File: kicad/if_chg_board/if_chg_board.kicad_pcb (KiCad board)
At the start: 2 copper layers, 62 x 26 mm, 46 parts, among them J1 USB_B_Micro, J2 B2B-ZH, J3 B2B-ZH, J4 Conn_01x05, Q1 SS8050-G, Q2 SS8050-G, SW1 B3U-1000P, SW2 B3U-1000P, U1 AMS1117-3.3, U2 LTC4054ES5-4.2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

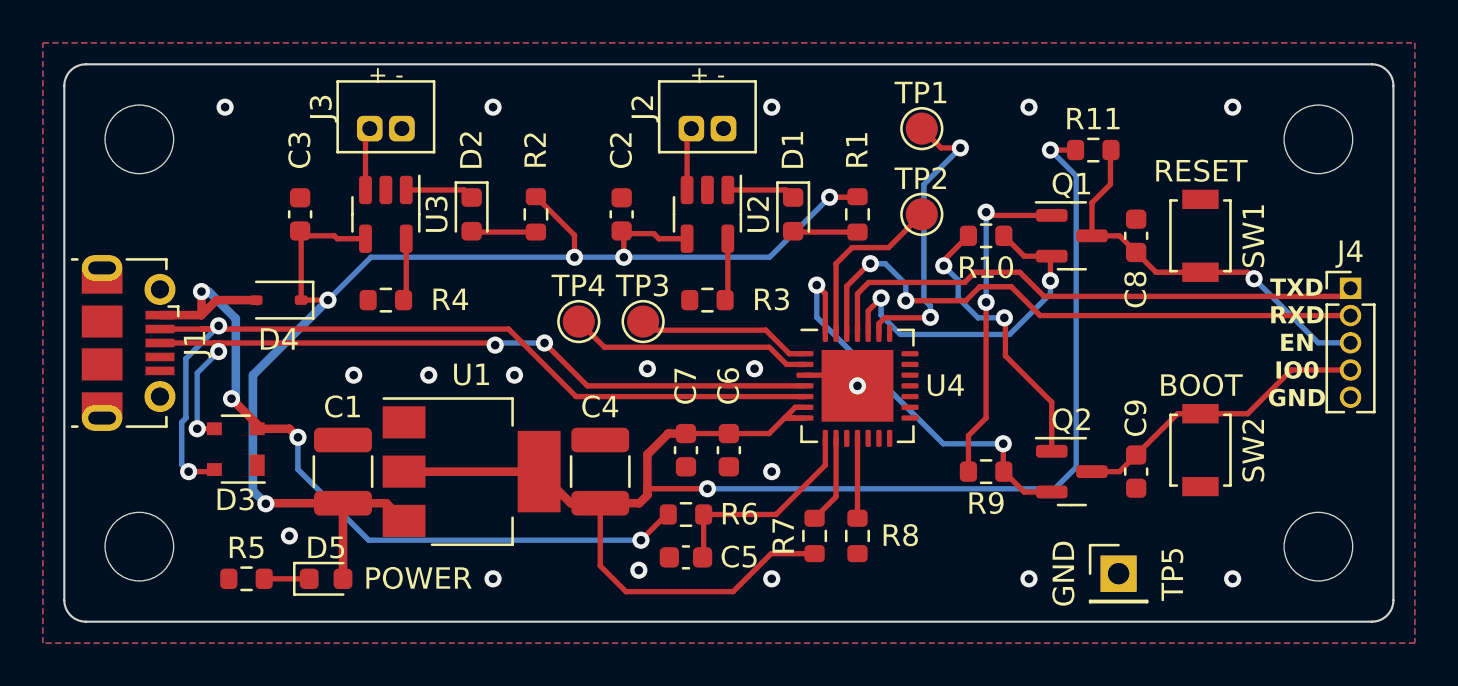
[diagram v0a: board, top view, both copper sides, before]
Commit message: Update if_chg_board
Signed-off-by: Kazuki Iida <elkel53930@gmail.com>
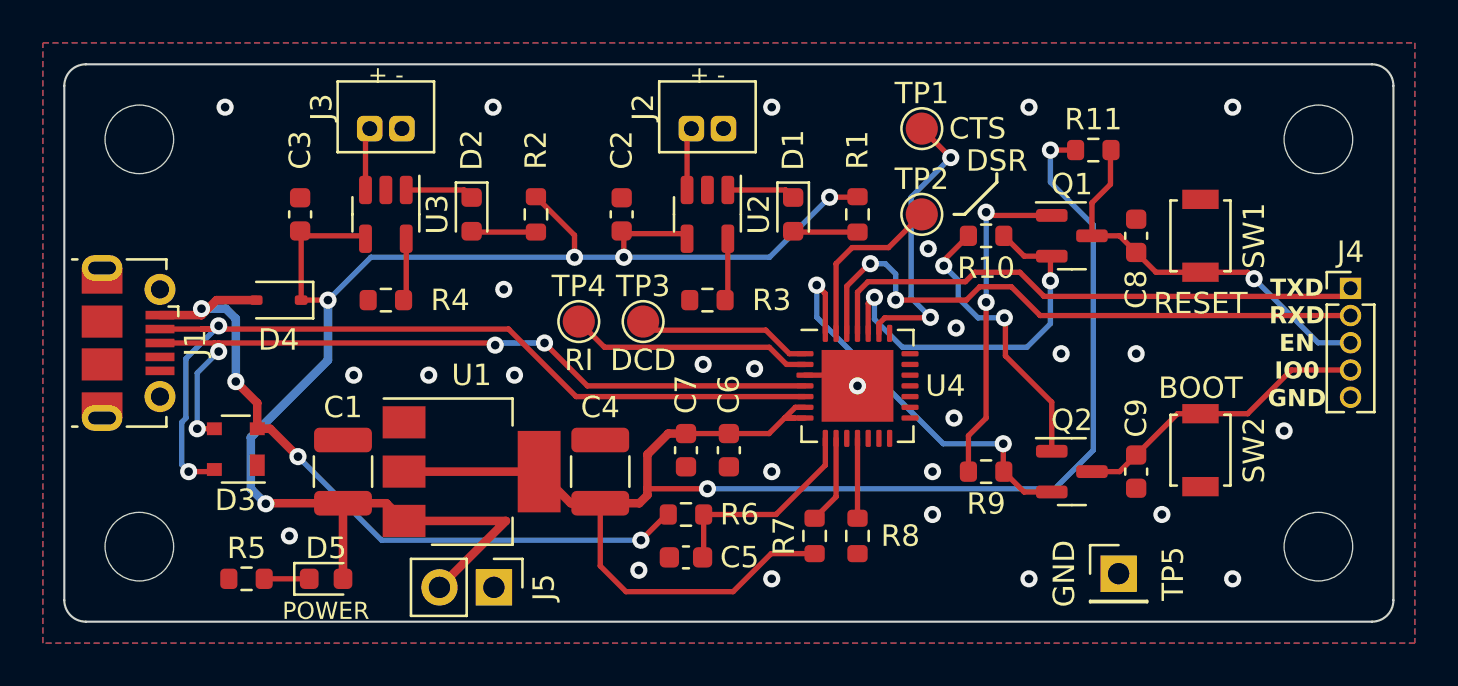
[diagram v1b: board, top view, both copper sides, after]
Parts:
- removed REF** (x4): MountingHole_3.2mm_M3, MountingHole:MountingHole_3.2mm_M3
- added H1: Φ3.2 M3, MountingHole:MountingHole_3.2mm_M3, F.Cu at (124.5, 91.5)
- added H2: Φ3.2 M3, MountingHole:MountingHole_3.2mm_M3, F.Cu at (124.5, 110.5)
- added H3: Φ3.2 M3, MountingHole:MountingHole_3.2mm_M3, F.Cu at (179.5, 91.5)
- added H4: Φ3.2 M3, MountingHole:MountingHole_3.2mm_M3, F.Cu at (179.5, 110.5)
- added J5: B2B-ZH, Connector_PinHeader_2.54mm:PinHeader_1x02_P2.54mm_Vertical, F.Cu at (141.0, 112.4)
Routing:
- net +5V: track 64.0 -> 73.2 mm
- net /VBUS: track 36.5 -> 34.2 mm
- net /RTS: track 16.2 -> 17.8 mm
- net +3.3V: track 74.7 -> 75.4 mm
- net GND: vias 18 -> 27
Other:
- board text added: "CTS"
- board text added: "DCD"
- board text added: "DSR"
- board text added: "RI"
